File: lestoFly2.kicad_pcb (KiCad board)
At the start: 2 copper layers, 35 x 40 mm, 43 parts, among them J1 Conn_01x02_Male, J10 Conn_01x07_Male, J2 Conn_01x06_Male, J3 Conn_Coaxial, J4 Micro_SD_Card_Det, J5 Conn_01x07_Male, J6 Conn_01x02_Male, J7 Conn_01x02_Male, J8 Conn_01x02_Male, J9 Conn_01x02_Male, Q1 DMN6140L, U1 NCP1117-1.8_TO252, U2 STM32H743ZITx, U3 ICM-20948, U4 ICM-20948, U5 RFM95W-868S2, U6 BMP280, Y1 25MHz

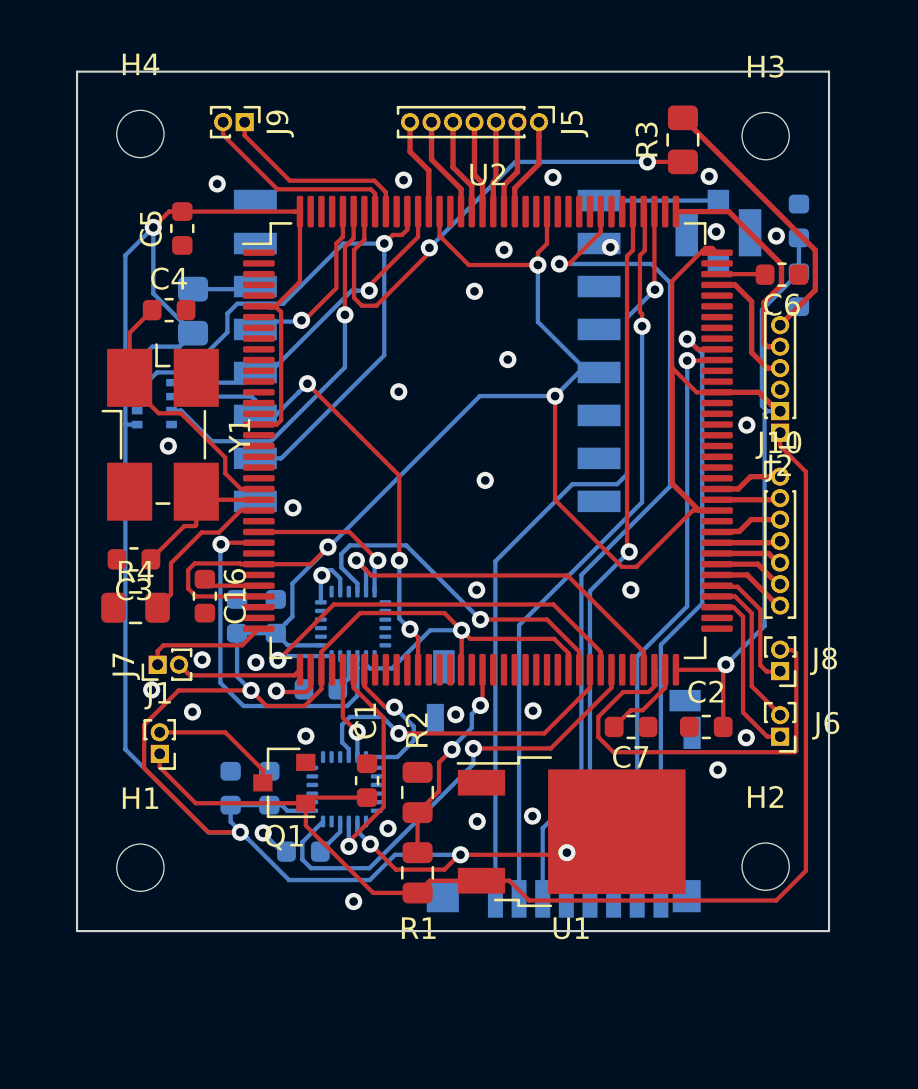
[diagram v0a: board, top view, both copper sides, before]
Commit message: fixed holes to be Naze32 compatible
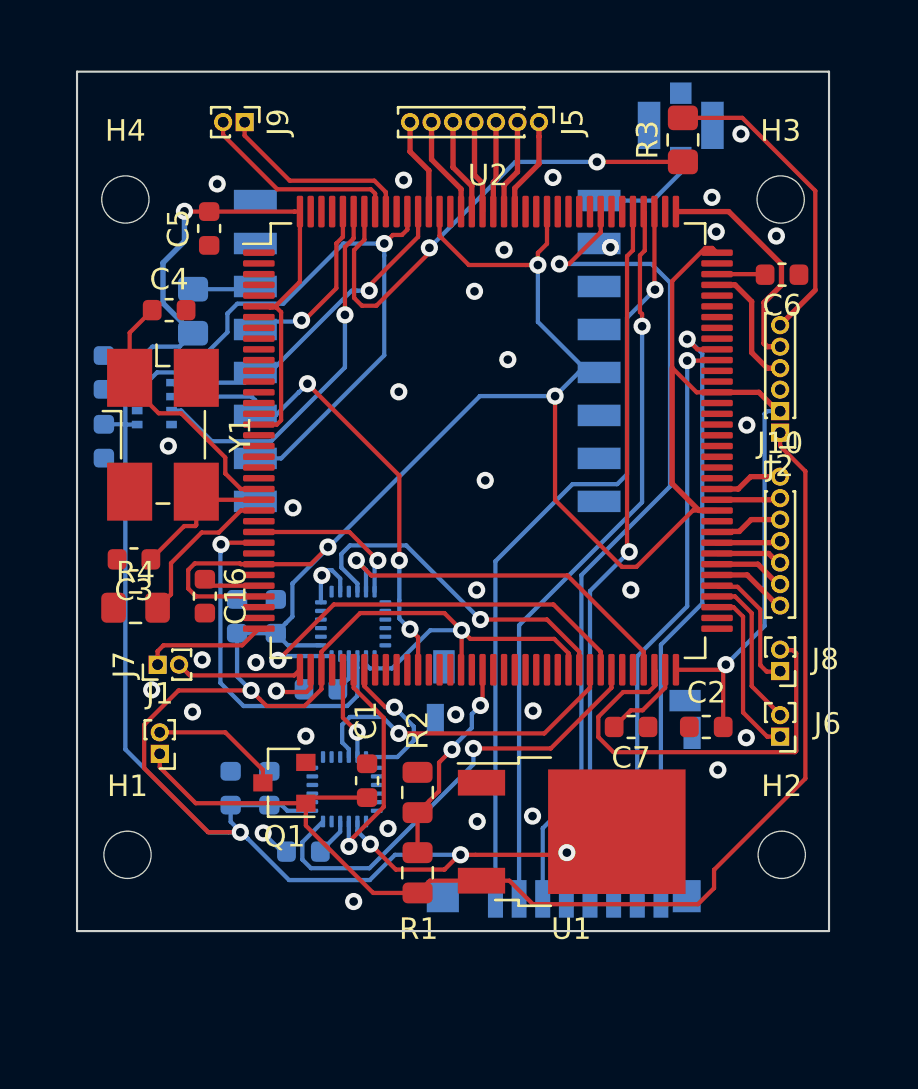
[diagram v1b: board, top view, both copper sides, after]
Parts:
- moved C14 33.1 mm to (79.0, 79.1)
- moved C15 33.1 mm to (79.0, 82.3)
- moved J3 5.30 mm to (105.8, 67.6), turned to 180 degrees
- moved H4 3.13 mm to (80.0, 71.0)
- moved H3 3.03 mm to (110.5, 71.0)
- moved C5 1.25 mm to (83.9, 72.4)
- moved H2 0.93 mm to (110.5, 101.5)
- moved H1 0.85 mm to (80.1, 101.5)
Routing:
- net +1V8: track 255.4 -> 239.6 mm
- net VCC: track 58.8 -> 56.9 mm
- net Net-(J2-Pad6): track 12.9 -> 14.5 mm
- net Net-(J3-Pad1): track 5.55 -> 5.04 mm
- net GND: vias 33 -> 34

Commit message: varius fixes
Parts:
- removed the C16 at (83.7, 89.5)
- removed the J2 at (110.5, 81.9)
- removed the J7 at (81.5, 92.7)
- removed Q1: DMN6140L, Package_TO_SOT_SMD:SOT-23
- removed Y1: 25MHz, Crystal:Crystal_SMD_0603-4Pin_6.0x3.5mm_HandSoldering
- added C1: 100nF, Capacitor_SMD:C_0603_1608Metric, F.Cu at (90.2, 73.7)
- added C14: 100nF, Capacitor_SMD:C_0603_1608Metric, F.Cu at (106.2, 83.8)
- added C19: 100nF, Capacitor_SMD:C_0603_1608Metric, F.Cu at (79.9, 90.4)
- added C2: 100nF, Capacitor_SMD:C_0603_1608Metric, F.Cu at (104.8, 75.8)
- added C20: 1nF, Capacitor_SMD:C_0603_1608Metric, F.Cu at (94.5, 101.5)
- added C22: 100nF, Capacitor_SMD:C_0603_1608Metric, B.Cu at (102.8, 97.4)
- added C23: 100nF, Capacitor_SMD:C_0603_1608Metric, B.Cu at (103.3, 94.1)
- added C25: 100nF, Capacitor_SMD:C_0603_1608Metric, B.Cu at (100.6, 96.7)
- added C26: 100nF, Capacitor_SMD:C_0603_1608Metric, B.Cu at (109.8, 74.9)
- added C27: 1uF, Capacitor_SMD:C_0603_1608Metric, B.Cu at (109.8, 77.9)
- added C28: 100nF, Capacitor_SMD:C_0603_1608Metric, B.Cu at (98.2, 85.1)
- added C29: 100nF, Capacitor_SMD:C_0603_1608Metric, B.Cu at (96.2, 85.8)
- added C30: 100nF, Capacitor_SMD:C_0603_1608Metric, B.Cu at (100.0, 89.3)
- added C6: 100nF, Capacitor_SMD:C_0603_1608Metric, F.Cu at (79.9, 85.4)
- added C7: 100nF, Capacitor_SMD:C_0603_1608Metric, F.Cu at (79.9, 91.9)
- added D1: D, Diode_SMD:D_1210_3225Metric, B.Cu at (94.4, 101.6)
- added F1: Polyfuse, Fuse:Fuse_1210_3225Metric, B.Cu at (91.2, 101.6)
- added J5: Conn_01x02_Male, Connector_PinHeader_1.00mm:PinHeader_1x02_P1.00mm_Vertical, F.Cu at (78.8, 97.8)
- added J8: Conn_01x02_Male, Connector_PinHeader_1.00mm:PinHeader_1x02_P1.00mm_Vertical, F.Cu at (86.8, 102.7)
- added R10: 47ohm, Resistor_SMD:R_0603_1608Metric, F.Cu at (79.9, 94.9)
- added R11: 47ohm, Resistor_SMD:R_0603_1608Metric, F.Cu at (108.8, 95.2)
- added R12: 47ohm, Resistor_SMD:R_0603_1608Metric, F.Cu at (108.8, 96.7)
- added R2: 10K, Resistor_SMD:R_0603_1608Metric, F.Cu at (79.9, 88.9)
- added R3: 47ohm, Resistor_SMD:R_0603_1608Metric, F.Cu at (108.8, 79.5)
- added R5: 1.5k, Resistor_SMD:R_0603_1608Metric, F.Cu at (84.0, 69.8)
- added R6: 1.5k, Resistor_SMD:R_0603_1608Metric, F.Cu at (84.0, 71.4)
- added R7: 47ohm, Resistor_SMD:R_0603_1608Metric, F.Cu at (108.8, 92.2)
- added R8: 47ohm, Resistor_SMD:R_0603_1608Metric, F.Cu at (108.8, 93.7)
- added R9: 47ohm, Resistor_SMD:R_0603_1608Metric, F.Cu at (81.6, 97.5)
- C10, C11, C12, C13, C8, C9: moved to F.Cu
- C21: renamed from C1; footprint Capacitor_SMD:C_0603_1608Metric -> Resistor_SMD:R_0805_2012Metric
- C3, C4: value 3.9pF -> 100nF
- J1: value Conn_01x02_Male -> Conn_01x05_Male; footprint Connector_PinHeader_1.00mm:PinHeader_1x02_P1.00mm_Vertical -> Connector_PinHeader_1.00mm:PinHeader_1x05_P1.00mm_Vertical
- R1: renamed from R3; footprint Resistor_SMD:R_0805_2012Metric_Pad1.15x1.40mm_HandSolder -> Resistor_SMD:R_0603_1608Metric
- R13: renamed from R5; footprint Resistor_SMD:R_0805_2012Metric_Pad1.15x1.40mm_HandSolder -> Resistor_SMD:R_0603_1608Metric
- R14: renamed from R1; footprint Resistor_SMD:R_0805_2012Metric -> Resistor_SMD:R_0603_1608Metric
- R15: renamed from R2; footprint Resistor_SMD:R_0805_2012Metric -> Resistor_SMD:R_0603_1608Metric
- R4: value 10K -> 47ohm; footprint Resistor_SMD:R_0805_2012Metric_Pad1.15x1.40mm_HandSolder -> Resistor_SMD:R_0603_1608Metric
- U1: value NCP1117-1.8_TO252 -> STM32H743ZITx; footprint Package_TO_SOT_SMD:TO-252-2 -> Package_QFP:LQFP-144_20x20mm_P0.5mm
- U2: value STM32H743ZITx -> RFM95W-868S2; footprint Package_QFP:LQFP-144_20x20mm_P0.5mm -> RF_Module:HOPERF_RFM9XW_SMD; moved to B.Cu
- U4: value ICM-20948 -> R-78C1.8-1.0; footprint Sensor_Motion:InvenSense_QFN-24_3x3mm_P0.4mm -> Converter_DCDC:Converter_DCDC_RECOM_R-78E-0.5_THT; moved to F.Cu
- U5: value RFM95W-868S2 -> ICM-20948; footprint RF_Module:HOPERF_RFM9XW_SMD -> Sensor_Motion:InvenSense_QFN-24_3x3mm_P0.4mm
- moved J1 34.5 mm to (111.5, 79.7)
- moved R4 31.5 mm to (108.9, 76.5), turned to 180 degrees
- moved J9 26.3 mm to (81.1, 76.3)
- moved J10 22.2 mm to (102.1, 76.1), turned to 0 degrees
- moved R13 21.9 mm to (84.6, 98.1), turned to 0 degrees
- moved C3 21.4 mm to (95.8, 73.0), turned to 270 degrees
- moved C13 21.0 mm to (106.2, 89.4), turned to 180 degrees
- moved C12 17.7 mm to (103.1, 98.0)
- moved U4 17.7 mm to (104.5, 101.8)
- moved U1 16.3 mm to (93.1, 86.2)
- moved C24 13.4 mm to (94.4, 100.0)
- moved U5 11.7 mm to (97.2, 89.3)
- moved U2 11.6 mm to (86.8, 88.1), turned to 90 degrees
- moved C8 11.6 mm to (79.9, 93.4), turned to 0 degrees
- moved U3 11.4 mm to (100.6, 93.9), turned to 270 degrees
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- renumbered C6 to C15, C7 to C16, C2 to C24, C14 to C31, C15 to C32, J4 to J10, J5 to J2, J10 to J3, J6 to J4, J8 to J6, J9 to J7, J3 to J9
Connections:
- C10 pad 1: +1V8 -> GND
- C10 pad 2: GND -> +1V8
- C11 pad 1: Net-(C11-Pad1) -> GND
- C11 pad 2: GND -> +1V8
- C12 pad 1: +1V8 -> GND
- C12 pad 2: GND -> +1V8
- C13 pad 1: +1V8 -> GND
- C13 pad 2: GND -> +1V8
- C3 pad 1: Net-(C3-Pad1) -> GND
- C3 pad 2: GND -> +1V8
- C4 pad 1: Net-(C4-Pad1) -> GND
- C4 pad 2: GND -> +1V8
- C8 pad 1: Net-(C8-Pad1) -> GND
- C8 pad 2: GND -> +1V8
- C9 pad 1: +1V8 -> GND
- C9 pad 2: GND -> +1V8
- J1 pad 1: VCC -> +1V8
- J1 pad 2: Net-(J1-Pad2) -> GND
- J2 pad 1: Net-(J5-Pad1) -> Net-(J2-Pad1)
- J2 pad 2: Net-(J5-Pad2) -> Net-(J2-Pad2)
- J2 pad 3: Net-(J5-Pad3) -> Net-(J2-Pad3)
- J2 pad 4: Net-(J5-Pad4) -> Net-(J2-Pad4)
- J2 pad 5: Net-(J5-Pad5) -> Net-(J2-Pad5)
- J2 pad 6: Net-(J5-Pad6) -> Net-(J2-Pad6)
- J2 pad 7: Net-(J5-Pad7) -> Net-(J2-Pad7)
- J3 pad 1: Net-(J10-Pad1) -> Net-(J3-Pad1)
- J3 pad 2: Net-(J10-Pad2) -> Net-(J3-Pad2)
- J3 pad 3: Net-(J10-Pad3) -> Net-(J3-Pad3)
- J3 pad 4: Net-(J10-Pad4) -> Net-(J3-Pad4)
- J3 pad 5: Net-(J10-Pad5) -> Net-(J3-Pad5)
- J3 pad 6: Net-(J10-Pad6) -> Net-(J3-Pad6)
- J3 pad 7: Net-(J10-Pad7) -> Net-(J3-Pad7)
- J4 pad 1: USART1_TX -> Net-(J4-Pad1)
- J4 pad 2: USART1_RX -> Net-(J4-Pad2)
- J6 pad 1: USART3_TX -> Net-(J6-Pad1)
- J6 pad 2: USART3_RX -> Net-(J6-Pad2)
- J9 pad 1: Net-(J3-Pad1) -> Net-(J9-Pad1)
- R1 pad 1: Net-(R3-Pad1) -> Net-(R1-Pad1)
- R1 pad 2: Net-(J2-Pad6) -> Net-(J1-Pad5)
- R13 pad 1: Net-(R5-Pad1) -> Net-(R13-Pad1)
- R4 pad 1: GND -> SWCLK
- U1 pad 1: GND -> Net-(U1-Pad1)
- U1 pad 2: +1V8 -> Net-(U1-Pad2)
- U1 pad 3: VCC -> Net-(U1-Pad3)
- U2 pad 1: Net-(U2-Pad1) -> GND
- U2 pad 10: Net-(U2-Pad10) -> GND
- U2 pad 13: Net-(U2-Pad13) -> +1V8
- U2 pad 16: GND -> Net-(U2-Pad16)
- U2 pad 2: Net-(U2-Pad2) -> SPI3_MISO
- U2 pad 3: Net-(U2-Pad3) -> SPI3_MOSI
- U2 pad 4: Net-(U2-Pad4) -> SPI3_CLK
- U2 pad 5: Net-(U2-Pad5) -> CS_LORA
- U2 pad 6: +1V8 -> Net-(R13-Pad1)
- U2 pad 8: Net-(U2-Pad8) -> GND
- U2 pad 9: Net-(U2-Pad9) -> Net-(J9-Pad1)
- U3 pad 10: Net-(C8-Pad1) -> Net-(C22-Pad1)
- U4 pad 1: Net-(U4-Pad1) -> VCC
- U4 pad 2: Net-(U4-Pad2) -> GND
- U4 pad 3: Net-(U4-Pad3) -> +1V8
- U5 pad 1: GND -> Net-(U5-Pad1)
- U5 pad 10: GND -> Net-(C28-Pad1)
- U5 pad 12: Net-(U5-Pad12) -> INT_IMU2
- U5 pad 2: SPI3_MISO -> Net-(U5-Pad2)
- U5 pad 3: SPI3_MOSI -> Net-(U5-Pad3)
- U5 pad 4: SPI3_CLK -> Net-(U5-Pad4)
- U5 pad 5: CS_LORA -> Net-(U5-Pad5)
- U5 pad 6: Net-(R5-Pad1) -> Net-(U5-Pad6)
- U5 pad 8: GND -> +1V8
- U5 pad 9: Net-(J3-Pad1) -> SPI2_MISO
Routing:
- net +1V8: track 239.6 -> 94.7 mm, vias 11 -> 17
- net VCC: track 56.9 -> 22.0 mm, vias 0 -> 1
- net Net-(R1-Pad1): track 0.00 -> 33.3 mm, vias 0 -> 2
- net SDMMC1_CMD: track 40.1 -> 8.43 mm
- net SDMMC1_D2: track 36.3 -> 8.43 mm
- net SDMMC1_CK: track 32.9 -> 5.16 mm
- net SDMMC1_D3: track 34.5 -> 7.44 mm
- net GND: track 6.70 -> 30.1 mm, vias 34 -> 8
- net Net-(R3-Pad1): track 22.6 -> 0.00 mm, vias 2 -> 0
- net CS_LORA: track 7.95 -> 22.6 mm
- net SPI1_MISO: track 10.6 -> 24.6 mm
- net Net-(C4-Pad1): track 12.4 -> 0.00 mm
- net SPI3_CLK: track 16.1 -> 27.6 mm
- net CS_IMU1: track 15.4 -> 3.94 mm
- net SPI1_CLK: track 4.34 -> 15.5 mm
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- added copper zone on In1.Cu, net +1V8
- added copper zone on In2.Cu, net GND
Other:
- board size 35 x 40 mm -> 35 x 35.6 mm
- copper layers 2 -> 4
